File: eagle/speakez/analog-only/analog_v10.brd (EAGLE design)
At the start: 46.2 x 48.3 mm, 46 parts, among them U1 +12v, U2 MAX5486

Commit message: made some more progress, shrunk the board
going to eat breakfast. yay first allnighter of 2.009
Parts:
- moved C15 26.5 mm to (43.7, 51.3)
- moved R18 24.7 mm to (43.7, 48.0)
- moved R26 5.24 mm to (26.7, 22.9), turned to 270 degrees
- moved R27 2.69 mm to (24.1, 22.9)
- moved HP 2.46 mm to (23.8, 45.5), turned to 270 degrees
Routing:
- net HP_R_AMPD: track 1.62 -> 23.3 mm, vias 0 -> 2
- net RIGHT: track 0.00 -> 15.7 mm
- net LEFT: track 0.00 -> 13.4 mm
- net HP_L_AMPD: track 0.00 -> 10.8 mm
- net GND: track 38.4 -> 43.8 mm, vias 18 -> 16
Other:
- board size 46.2 x 48.3 mm -> 43.7 x 45.7 mm
- board text added: "+"
- board text added: "-"

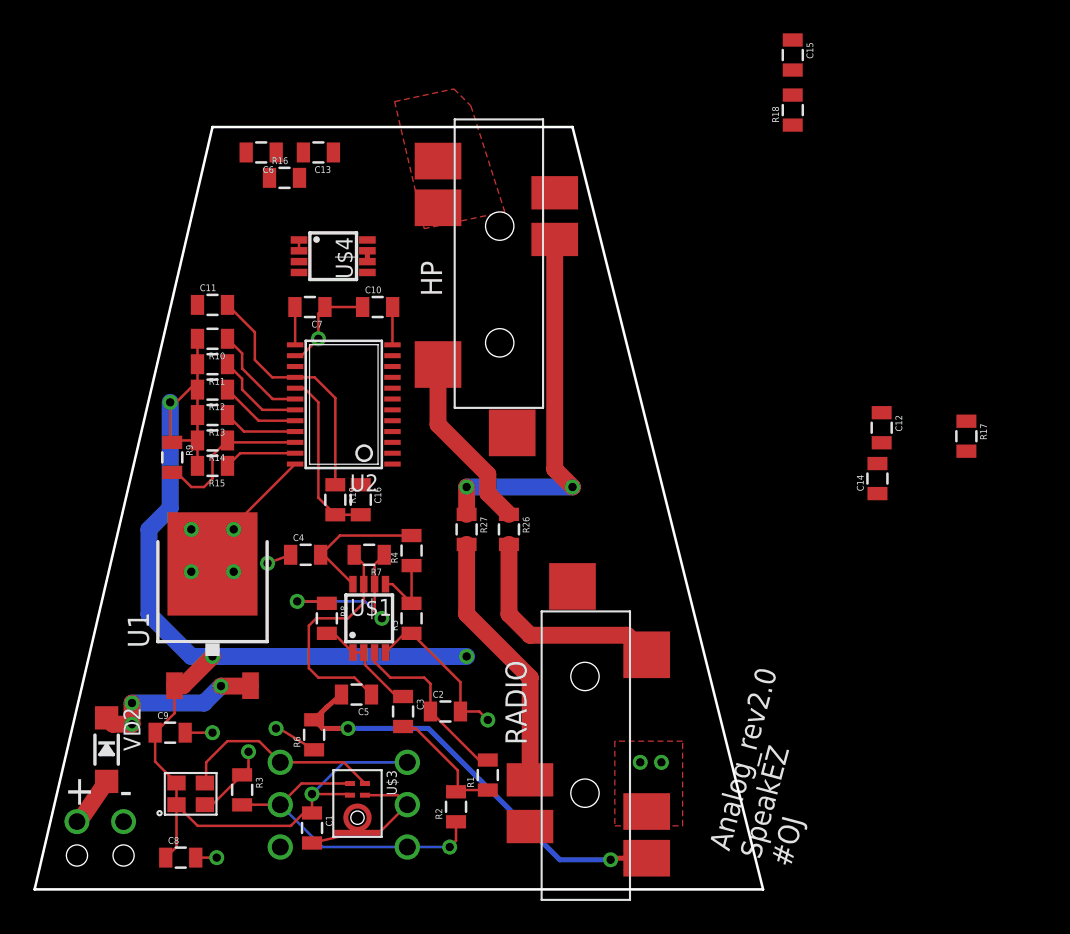
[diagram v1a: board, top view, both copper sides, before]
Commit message: arranged the offsetters
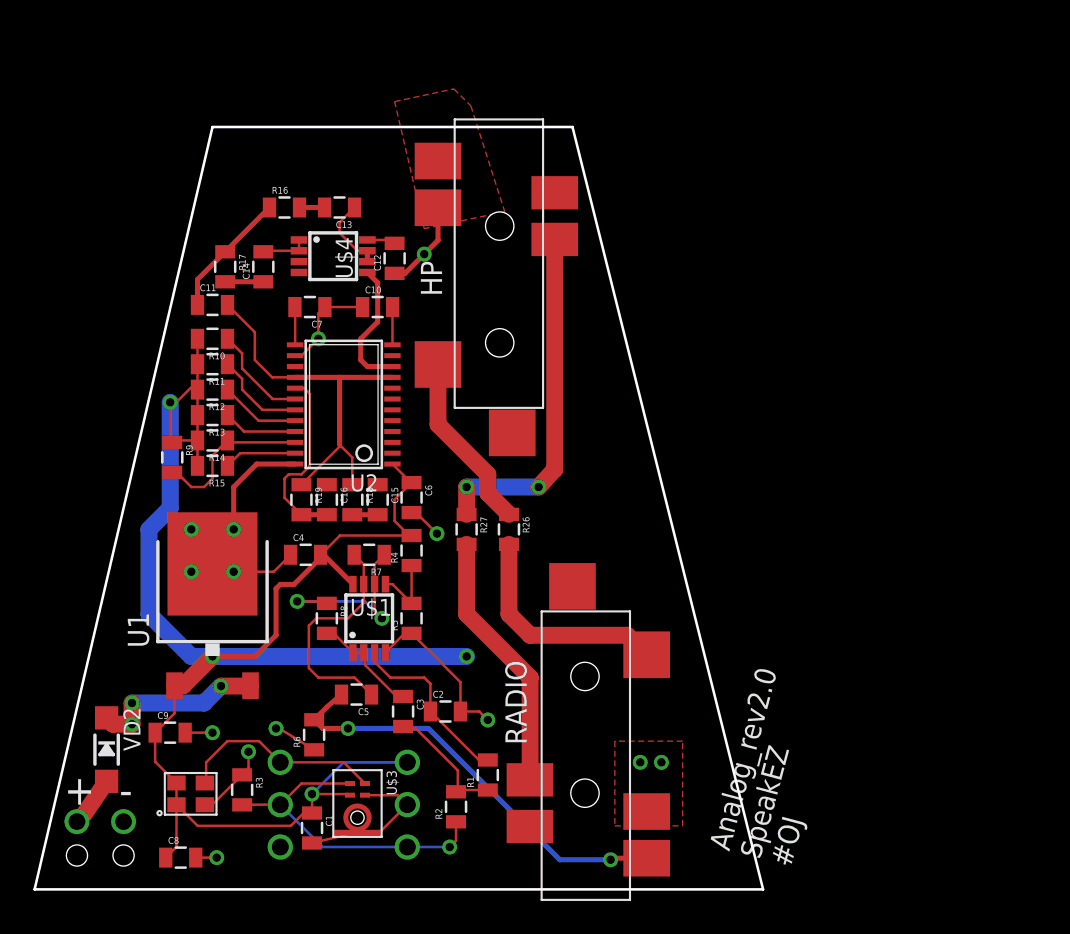
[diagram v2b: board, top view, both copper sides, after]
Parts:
- moved R17 45.6 mm to (9.65, 38.6)
- moved C14 39.0 mm to (11.9, 38.6)
- moved C15 36.5 mm to (18.8, 24.6)
- moved R18 35.3 mm to (17.3, 24.6), turned to 270 degrees
- moved C12 30.9 mm to (19.8, 39.1), turned to 90 degrees
- moved C6 22.6 mm to (20.8, 24.8), turned to 270 degrees
- moved C13 3.54 mm to (16.5, 42.2)
- moved C16 2.03 mm to (15.7, 24.6)
- moved R19 2.03 mm to (14.2, 24.6)
- moved R16 1.78 mm to (13.2, 42.2)
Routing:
- net GND: track 43.8 -> 62.6 mm, vias 16 -> 17
- net VCC: track 91.6 -> 109.8 mm
- net HEADPH_R: track 0.00 -> 7.99 mm
- net BIAS: track 15.0 -> 22.8 mm
- net N$10: track 0.65 -> 4.66 mm
- net HP_L_AMPD: track 10.8 -> 13.0 mm
- net N$14: track 0.65 -> 2.82 mm
- net RIGHT_OFFSET: track 0.00 -> 1.52 mm
- net LEFT_OFFSET: track 10.4 -> 11.3 mm
- net HP_R_AMPD: track 23.3 -> 22.7 mm

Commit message: tweaking things, clearing out some clearance errors
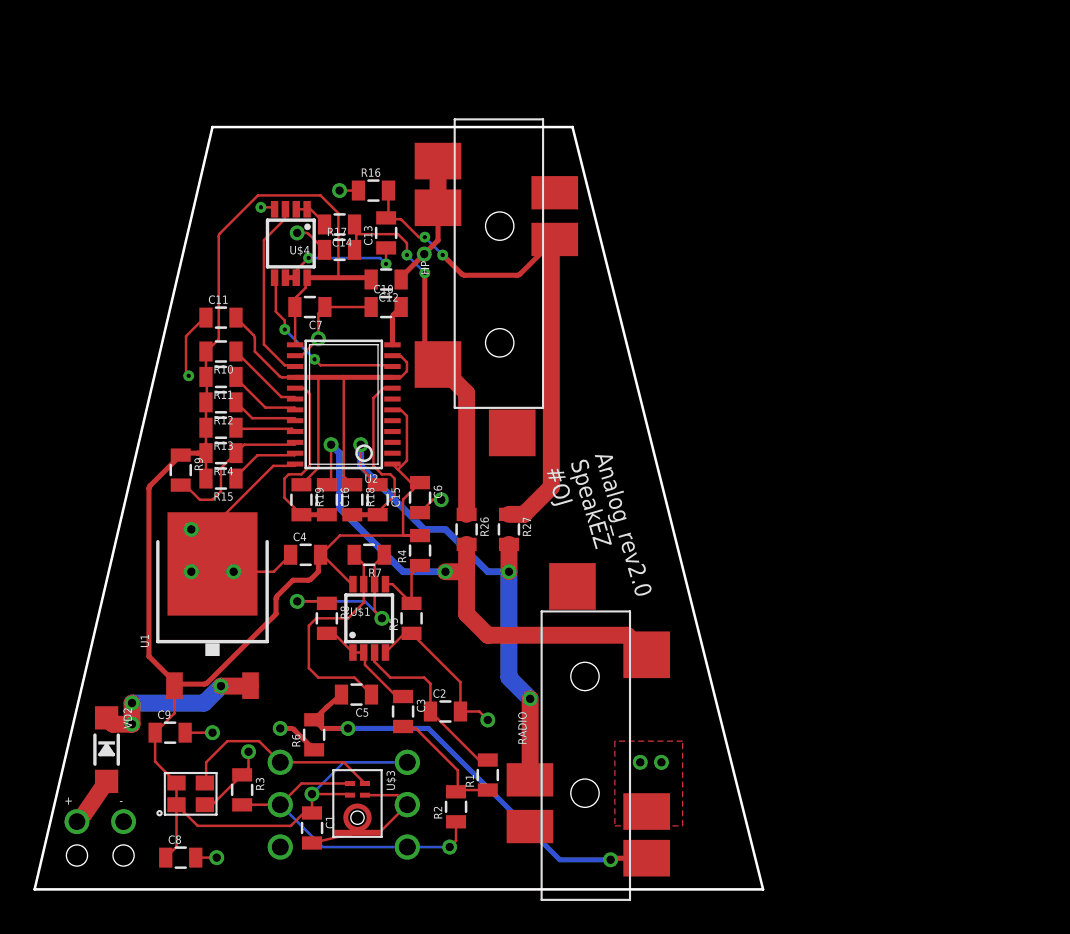
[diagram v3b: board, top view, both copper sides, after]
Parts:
- VD2: value (none) -> 40V AF DIODE
- moved R17 6.93 mm to (16.5, 39.6), turned to 0 degrees
- moved R16 5.43 mm to (18.5, 43.2)
- moved C14 5.23 mm to (16.5, 41.1), turned to 180 degrees
- moved C13 3.18 mm to (19.3, 40.6), turned to 90 degrees
- moved U$4 2.65 mm to (13.6, 40.0), turned to 180 degrees
- moved R26 2.54 mm to (24.1, 22.9)
- moved R27 2.54 mm to (26.7, 22.9)
- moved C12 1.37 mm to (19.3, 37.8), turned to 180 degrees
- moved R9 0.92 mm to (6.99, 26.4)
- moved C11 0.92 mm to (9.40, 35.6)
- moved R10 0.92 mm to (9.40, 33.5)
- moved R11 0.92 mm to (9.40, 32.0)
- moved R12 0.92 mm to (9.40, 30.5)
- moved R13 0.92 mm to (9.40, 29.0)
- moved R14 0.92 mm to (9.40, 27.4)
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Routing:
- net LEFT: track 13.4 -> 31.7 mm, vias 0 -> 2
- net RIGHT: track 15.7 -> 30.3 mm, vias 0 -> 3
- net HEADPH_L: track 0.00 -> 11.1 mm
- net HP_L_AMPD: track 13.0 -> 23.2 mm, vias 0 -> 2
- net RIGHT_OFFSET: track 1.52 -> 11.2 mm
- net HP_R_AMPD: track 22.7 -> 31.9 mm
- net VCC: track 109.8 -> 116.8 mm, vias 5 -> 2
- net GND: track 62.6 -> 69.4 mm, vias 17 -> 20
- net BIAS: track 22.8 -> 27.4 mm
- net N$10: track 4.66 -> 7.99 mm, vias 0 -> 2
- net HEADPH_R: track 7.99 -> 10.8 mm, vias 0 -> 2
- net N$5: track 6.08 -> 4.77 mm
- net N$6: track 5.57 -> 4.45 mm
- net N$9: track 4.47 -> 3.66 mm
- net N$8: track 4.83 -> 4.06 mm
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
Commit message: fixed all clearance issues, unsure about some dimensions issues
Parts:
- moved C8 1.20 mm to (8.00, 3.81)
- moved C5 0.25 mm to (17.3, 13.0)
- moved VD2 0.13 mm to (2.67, 9.65)
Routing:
- net NO_DN: track 0.00 -> 17.2 mm, vias 0 -> 2
- net NO_UP: track 0.00 -> 13.9 mm, vias 0 -> 2
- net NO_MUTE: track 0.00 -> 13.0 mm, vias 0 -> 2
- net MIC_PDM: track 19.9 -> 21.1 mm
- net VBAT: track 3.05 -> 2.03 mm
- net GND: track 69.4 -> 70.0 mm

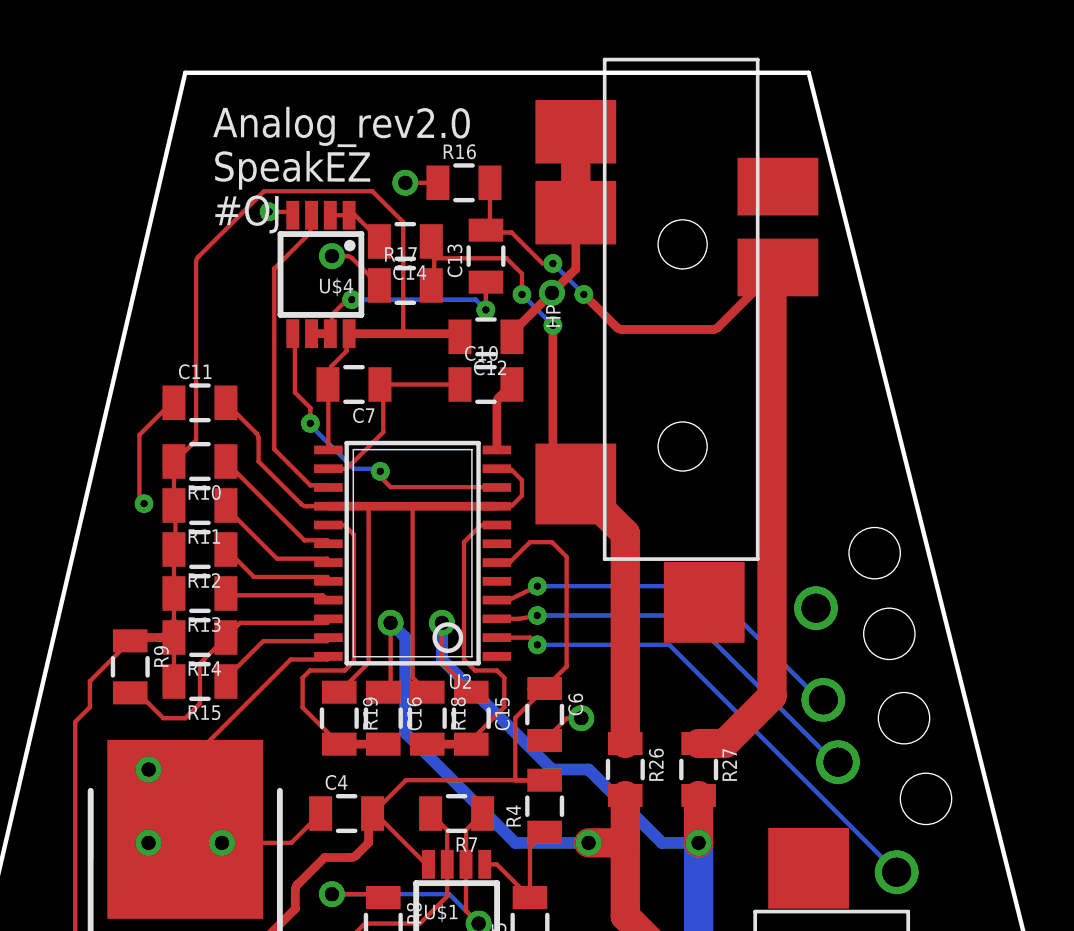
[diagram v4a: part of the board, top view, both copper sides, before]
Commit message: got rid of mute + headphone jack; added solder holes + strain relief
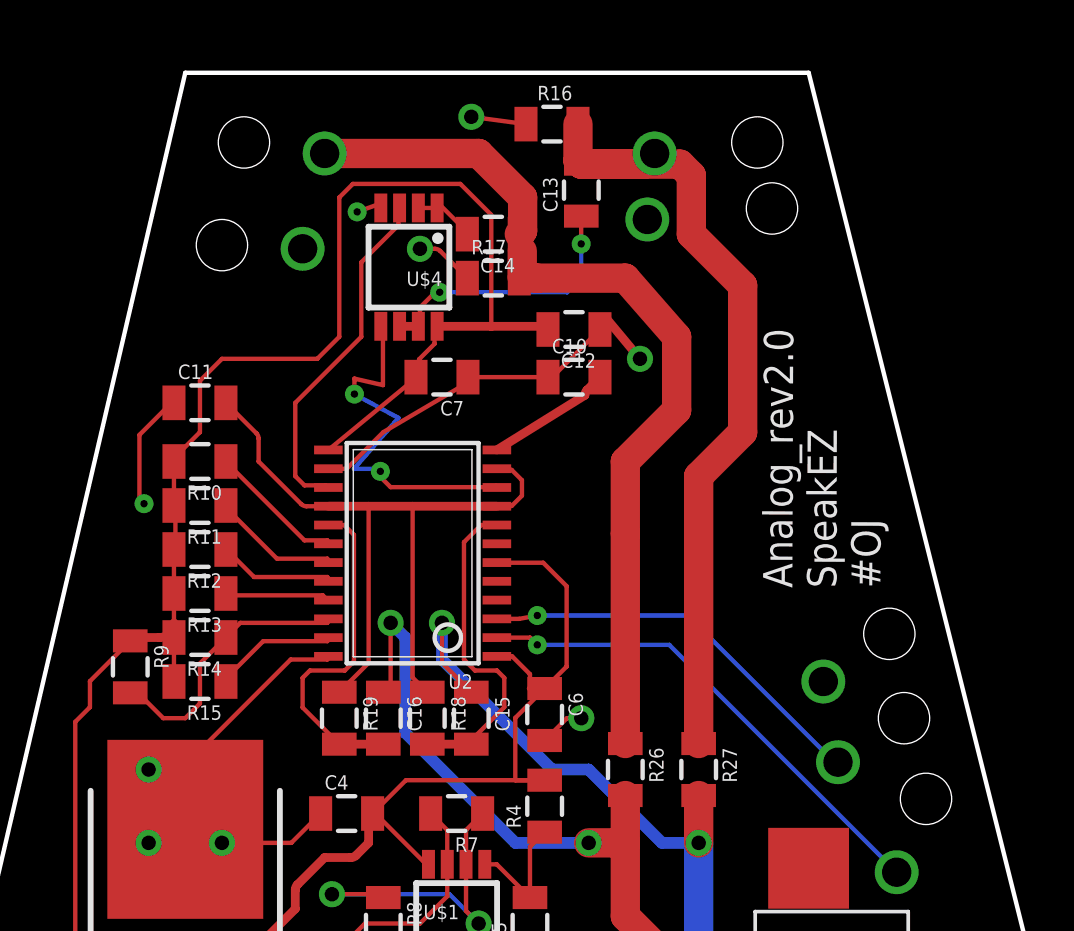
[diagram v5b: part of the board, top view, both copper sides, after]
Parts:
- removed HP: SJ-43514-SMT, 35mm_audio:35MM_SMD_4WIRE
- moved C13 4.02 mm to (22.6, 42.9)
- moved R16 3.66 mm to (21.6, 45.2)
- moved C12 3.06 mm to (22.4, 38.1)
- moved C10 3.06 mm to (22.4, 36.4)
- moved C7 3.06 mm to (17.8, 36.4)
- moved U$4 3.06 mm to (16.6, 40.3)
- moved C14 3.06 mm to (19.6, 41.4)
- moved R17 3.06 mm to (19.6, 39.9)
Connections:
- net GND: no longer HP.P$1, HP.P$4
- net HP_L_AMPD: no longer HP.P$2
- net HP_R_AMPD: no longer HP.P$3
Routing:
- net NO_MUTE: track 13.0 -> 0.41 mm, vias 2 -> 0
- net HP_L_AMPD: track 23.2 -> 33.5 mm, vias 2 -> 1
- net VCC: track 116.4 -> 122.3 mm
- net HP_R_AMPD: track 31.9 -> 29.1 mm, vias 2 -> 1
- net HEADPH_R: track 11.0 -> 13.1 mm
- net N$12: track 2.47 -> 4.42 mm
- net N$10: track 8.43 -> 9.93 mm
- net HEADPH_L: track 11.1 -> 12.1 mm
- net GND: track 70.0 -> 69.6 mm, vias 20 -> 22

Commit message: routing tweaks
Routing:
- net HEADPH_R: track 13.1 -> 9.70 mm

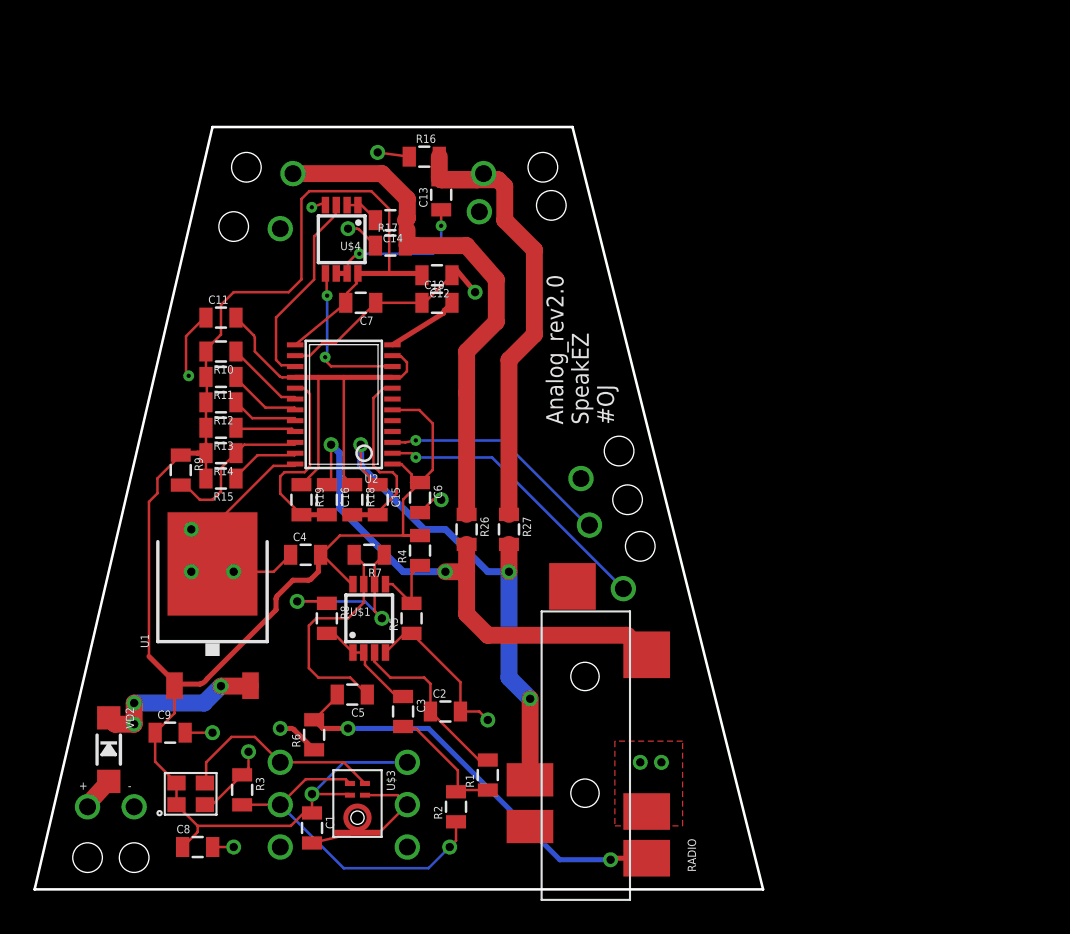
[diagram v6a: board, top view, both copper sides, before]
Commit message: fattened up traces
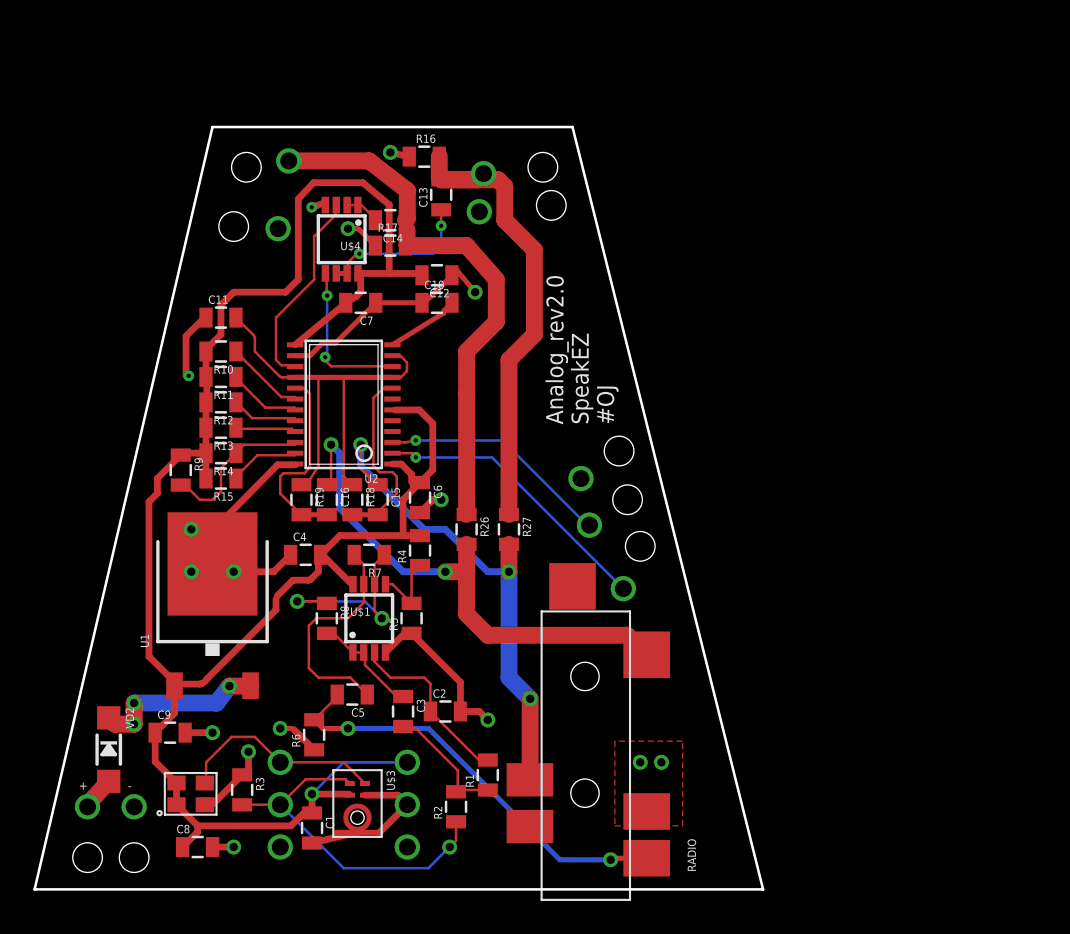
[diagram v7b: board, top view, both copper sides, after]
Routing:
- net VCC: track 122.3 -> 123.1 mm
- net HP_L_AMPD: track 33.5 -> 34.2 mm
- net GND: track 69.7 -> 69.0 mm
